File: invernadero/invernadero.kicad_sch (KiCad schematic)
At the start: 0 parts

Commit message: placa con conexiones para display y botonera
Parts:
- added J1, J2: Conn_02x20_Odd_Even, Connector_PinSocket_2.54mm:PinSocket_2x20_P2.54mm_Vertical, symbol Connector_Generic:Conn_02x20_Odd_Even
- added J3: Conn_01x08_Pin, Connector_PinHeader_2.54mm:PinHeader_1x08_P2.54mm_Vertical, symbol Connector:Conn_01x08_Pin
- added J4: Conn_01x16_Socket, Connector_PinSocket_2.54mm:PinSocket_1x16_P2.54mm_Vertical, symbol Connector:Conn_01x16_Socket
- added R1: 1k, Resistor_THT:R_Axial_DIN0207_L6.3mm_D2.5mm_P10.16mm_Horizontal, symbol Device:R
- added RV1: R_Potentiometer_Trim, Potentiometer_THT:Potentiometer_Bourns_3386P_Vertical, symbol Device:R_Potentiometer_Trim
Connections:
- new net: J4.15 (Pin_15), R1.1
- new net: J4.3 (Pin_3), RV1.2
- new net: J1.3 (Pin_3), J3.1 (Pin_1)
- new net: J1.1 (Pin_1), J3.2 (Pin_2)
- new net: J1.2 (Pin_2), J3.3 (Pin_3)
- new net: J1.4 (Pin_4), J3.4 (Pin_4)
- new net: J1.36 (Pin_36), J3.5 (Pin_5)
- new net: J1.38 (Pin_38), J3.6 (Pin_6)
- new net: J1.37 (Pin_37), J3.7 (Pin_7)
- new net: J1.35 (Pin_35), J3.8 (Pin_8)
- new net +5V: J1.17 (Pin_17), J4.2 (Pin_2), R1.2, RV1.3
- new net GND: J1.20 (Pin_20), J1.7 (Pin_7), J2.10 (Pin_10), J2.19 (Pin_19), J4.1 (Pin_1), J4.16 (Pin_16), J4.5 (Pin_5), RV1.1
- new net PA8: J2.24 (Pin_24), J4.11 (Pin_11)
- new net PA9: J2.22 (Pin_22), J4.6 (Pin_6)
- new net PB10: J2.26 (Pin_26), J4.12 (Pin_12)
- new net PB4: J2.28 (Pin_28), J4.13 (Pin_13)
- new net PB5: J2.30 (Pin_30), J4.14 (Pin_14)
- new net PC7: J2.20 (Pin_20), J4.4 (Pin_4)
- no-connect marks 0 -> 6
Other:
- note added: "Display"

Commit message: Diseño de PCB completo
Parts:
- added D1: LED, LED_THT:LED_D4.0mm, symbol Device:LED
- added D2: D, Diode_THT:D_DO-41_SOD81_P7.62mm_Horizontal, symbol Device:D
- added J5: Conn_01x04_Socket, Connector_PinSocket_2.54mm:PinSocket_1x04_P2.54mm_Vertical, symbol Connector:Conn_01x04_Socket
- added J6, J7, J9: Conn_01x02_Socket, Connector_PinSocket_2.54mm:PinSocket_1x02_P2.54mm_Vertical, symbol Connector:Conn_01x02_Socket
- added J8: Conn_01x03_Socket, Connector_PinSocket_2.54mm:PinSocket_1x03_P2.54mm_Vertical, symbol Connector:Conn_01x03_Socket
- added Q1: NPN, Package_TO_SOT_THT:TO-92_Inline, symbol Simulation_SPICE:NPN
- added R2, R3: 3.3k, Resistor_THT:R_Axial_DIN0204_L3.6mm_D1.6mm_P5.08mm_Horizontal, symbol Device:R
- added R4: 27k, Resistor_THT:R_Axial_DIN0207_L6.3mm_D2.5mm_P7.62mm_Horizontal, symbol Device:R
- added R5: 1.2k, Resistor_THT:R_Axial_DIN0207_L6.3mm_D2.5mm_P7.62mm_Horizontal, symbol Device:R
- added R6, R7, R8: R, Resistor_THT:R_Axial_DIN0204_L3.6mm_D1.6mm_P5.08mm_Horizontal, symbol Device:R
- R1: footprint Resistor_THT:R_Axial_DIN0207_L6.3mm_D2.5mm_P10.16mm_Horizontal -> Resistor_THT:R_Axial_DIN0204_L3.6mm_D1.6mm_P5.08mm_Horizontal
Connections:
- net GND: now also D1.1 (K), J5.2 (Pin_2), J8.3 (Pin_3), Q1.3 (E), R4.2, R5.2, R8.2
- net PC8: now reaches J2.1 (Pin_1)
- net PC8: now also R6.1
- net PC9: now reaches J2.2 (Pin_2)
- net PC9: now also R7.1
- net PB8: now reaches J2.4 (Pin_4)
- net PB8: now also J5.3 (Pin_3), R3.2
- net PB9: now reaches J2.6 (Pin_6)
- net PB9: now also J5.4 (Pin_4), R2.2
- net PD2: now reaches J1.3 (Pin_3), J3.1 (Pin_1)
- net PC11: now reaches J1.1 (Pin_1), J3.2 (Pin_2)
- net PC10: now reaches J1.2 (Pin_2), J3.3 (Pin_3)
- net PC12: now reaches J1.4 (Pin_4), J3.4 (Pin_4)
- net PC2: now reaches J1.36 (Pin_36), J3.5 (Pin_5)
- net PC3: now reaches J1.38 (Pin_38), J3.6 (Pin_6)
- net PC0: now reaches J1.37 (Pin_37), J3.7 (Pin_7)
- net PC1: now reaches J1.35 (Pin_35), J3.8 (Pin_8)
- net +3.3V: now reaches J1.15 (Pin_15)
- net +3.3V: now also J5.1 (Pin_1), J6.1 (Pin_1), J7.1 (Pin_1), J8.2 (Pin_2), R2.1, R3.1
- net PA0: now reaches J1.27 (Pin_27)
- net PA0: now also J6.2 (Pin_2), R5.1
- net PA1: now reaches J1.29 (Pin_29)
- net PA1: now also J8.1 (Pin_1)
- net PA4: now reaches J1.31 (Pin_31)
- net PA4: now also J7.2 (Pin_2), R4.1
- new net: Q1.2 (B), R7.2, R8.1
- new net: D1.2 (A), R6.2
- new net: D2.2 (A), J9.2 (Pin_2), Q1.1 (C)
- new net +12V: D2.1 (K), J9.1 (Pin_1)
- no-connect marks 6 -> 8
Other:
- note added: "AT24C08"
- note added: "Humedad"
- note added: "Keypad"
- note added: "Luz"
- note added: "Sensores"
- note added: "Temperatura"
- moved on the sheet: J3, J4, R1, RV1

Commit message: esquemático
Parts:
- added J10: Conn_01x02_Socket, TerminalBlock_CUI:TerminalBlock_CUI_TB007-508-02_1x02_P5.08mm_Horizontal, symbol Connector:Conn_01x02_Socket
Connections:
- net +12V: now also J10.1 (Pin_1)
- net GND: now also J10.2 (Pin_2)
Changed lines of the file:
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@@
+	(wire
+		(pts
+			(xy 227.33 158.75) (xy 229.87 158.75)
+		)
+		(stroke
+			(width 0)
+			(type default)
+		)
+	)
 	(wire
 		(pts
@@
 		(pts
 			(xy 207.01 158.75) (xy 207.01 161.29)
+		)
+		(stroke
+			(width 0)
+			(type default)
+		)
+	)
+	(wire
+		(pts
+			(xy 227.33 156.21) (xy 229.87 156.21)
 		)
 		(stroke
@@
 	)
 	(symbol
+		(lib_id "Connector:Conn_01x02_Socket")
+		(at 234.95 156.21 0)
+		(unit 1)
+		(exclude_from_sim no)
+		(in_bom yes)
+		(on_board yes)
+		(dnp no)
+		(fields_autoplaced yes)
+		(property "Reference" "J10"
+			(at 235.6612 156.2678 0)
+			(effects
+				(font
+					(size 1.27 1.27)
+				)
+				(justify left)
+			)
+		)
+		(property "Value" "Conn_01x02_Socket"
+			(at 235.6612 158.6921 0)
+			(effects
+				(font
+					(size 1.27 1.27)
+				)
+				(justify left)
+			)
+		)
+		(property "Footprint" "TerminalBlock_CUI:TerminalBlock_CUI_TB007-508-02_1x02_P5.08mm_Horizontal"
+			(at 234.95 156.21 0)
+			(effects
+				(font
+					(size 1.27 1.27)
+				)
+				(hide yes)
+			)
+		)
+		(property "Datasheet" "~"
+			(at 234.95 156.21 0)
+			(effects
+				(font
+					(size 1.27 1.27)
+				)
+				(hide yes)
+			)
+		)
+		(property "Description" "Generic connector, single row, 01x02, script generated"
+			(at 234.95 156.21 0)
+			(effects
+				(font
+					(size 1.27 1.27)
+				)
+				(hide yes)
+			)
+		)
+		(pin "2"
+		)
+		(pin "1"
+		)
+		(instances
+			(project ""
+				(path "/aeacc457-9040-4f3b-92d7-10d03e7d1e75"
+					(reference "J10")
+					(unit 1)
+				)
+			)
+		)
+	)
+	(symbol
 		(lib_id "Device:R")
 		(at 177.8 137.16 0)
@@
 	)
 	(symbol
+		(lib_id "power:+12V")
+		(at 227.33 156.21 0)
+		(unit 1)
+		(exclude_from_sim no)
+		(in_bom yes)
+		(on_board yes)
+		(dnp no)
+		(fields_autoplaced yes)
+		(property "Reference" "#PWR025"
+			(at 227.33 160.02 0)
+			(effects
+				(font
+					(size 1.27 1.27)
+				)
+				(hide yes)
+			)
+		)
+		(property "Value" "+12V"
+			(at 227.33 152.0769 0)
+			(effects
+				(font
+					(size 1.27 1.27)
+				)
+			)
+		)
+		(property "Footprint" ""
+			(at 227.33 156.21 0)
+			(effects
+				(font
+					(size 1.27 1.27)
+				)
+				(hide yes)
+			)
+		)
+		(property "Datasheet" ""
+			(at 227.33 156.21 0)
+			(effects
+				(font
+					(size 1.27 1.27)
+				)
+				(hide yes)
+			)
+		)
+		(property "Description" "Power symbol creates a global label with name \"+12V\""
+			(at 227.33 156.21 0)
+			(effects
+				(font
+					(size 1.27 1.27)
+				)
+				(hide yes)
+			)
+		)
+		(pin "1"
+		)
+		(instances
+			(project "invernadero"
+				(path "/aeacc457-9040-4f3b-92d7-10d03e7d1e75"
+					(reference "#PWR025")
+					(unit 1)
+				)
+			)
+		)
+	)
+	(symbol
 		(lib_id "Device:R_Potentiometer_Trim")
 		(at 138.43 143.51 180)
@@
 					(unit 1)
 				)
+			)
+		)
+	)
+	(symbol
+		(lib_id "power:GND")
+		(at 227.33 158.75 0)
+		(unit 1)
+		(exclude_from_sim no)
+		(in_bom yes)
+		(on_board yes)
+		(dnp no)
+		(fields_autoplaced yes)
+		(property "Reference" "#PWR026"
+			(at 227.33 165.1 0)
+			(effects
+				(font
+					(size 1.27 1.27)
+				)
+				(hide yes)
+			)
+		)
+		(property "Value" "GND"
+			(at 227.33 162.8831 0)
+			(effects
+				(font
+					(size 1.27 1.27)
+				)
+			)
+		)
+		(property "Footprint" ""
+			(at 227.33 158.75 0)
+			(effects
+				(font
+					(size 1.27 1.27)
+				)
+				(hide yes)
+			)
+		)
+		(property "Datasheet" ""
+			(at 227.33 158.75 0)
+			(effects
+				(font
+					(size 1.27 1.27)
+				)
+				(hide yes)
+			)
+		)
+		(property "Description" "Power symbol creates a global label with name \"GND\" , ground"
+			(at 227.33 158.75 0)
+			(effects
+				(font
+					(size 1.27 1.27)
+				)
+				(hide yes)
+			)
+		)
+		(pin "1"
+		)
+		(instances
+			(project "invernadero"
+				(path "/aeacc457-9040-4f3b-92d7-10d03e7d1e75"
+					(reference "#PWR026")
+					(unit 1)
+				)

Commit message: cambios en el pcb
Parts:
- added R9: 220k, Resistor_THT:R_Axial_DIN0207_L6.3mm_D2.5mm_P7.62mm_Horizontal, symbol Device:R
- J9: footprint Connector_PinSocket_2.54mm:PinSocket_1x02_P2.54mm_Vertical -> TerminalBlock_CUI:TerminalBlock_CUI_TB007-508-02_1x02_P5.08mm_Horizontal
- R6: value R -> 3.3k
- R7, R8: value R -> 1k
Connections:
- net GND: now also R9.1; no longer R8.2
- net at R7.2, R8.1: no longer Q1.2 (B)
- new net: Q1.2 (B), R8.2, R9.2
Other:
- moved on the sheet: D2, J10, J9, Q1, R7, R8

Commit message: Modificado footprint de led y path de fan más ancho
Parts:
- D1: footprint LED_THT:LED_D4.0mm -> LED_THT:LED_D3.0mm_Clear
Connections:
- net fan-: now reaches D2.2 (A), J9.2 (Pin_2), Q1.1 (C)
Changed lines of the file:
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@@
+		)
+	)
+	(label "fan-"
+		(at 224.79 142.24 0)
+		(effects
+			(font
+				(size 1.27 1.27)
+			)
+			(justify left bottom)
 		)
 	)
@@
 			)
 		)
-		(property "Footprint" "LED_THT:LED_D4.0mm"
+		(property "Footprint" "LED_THT:LED_D3.0mm_Clear"
 			(at 177.8 147.32 0)
 			(effects

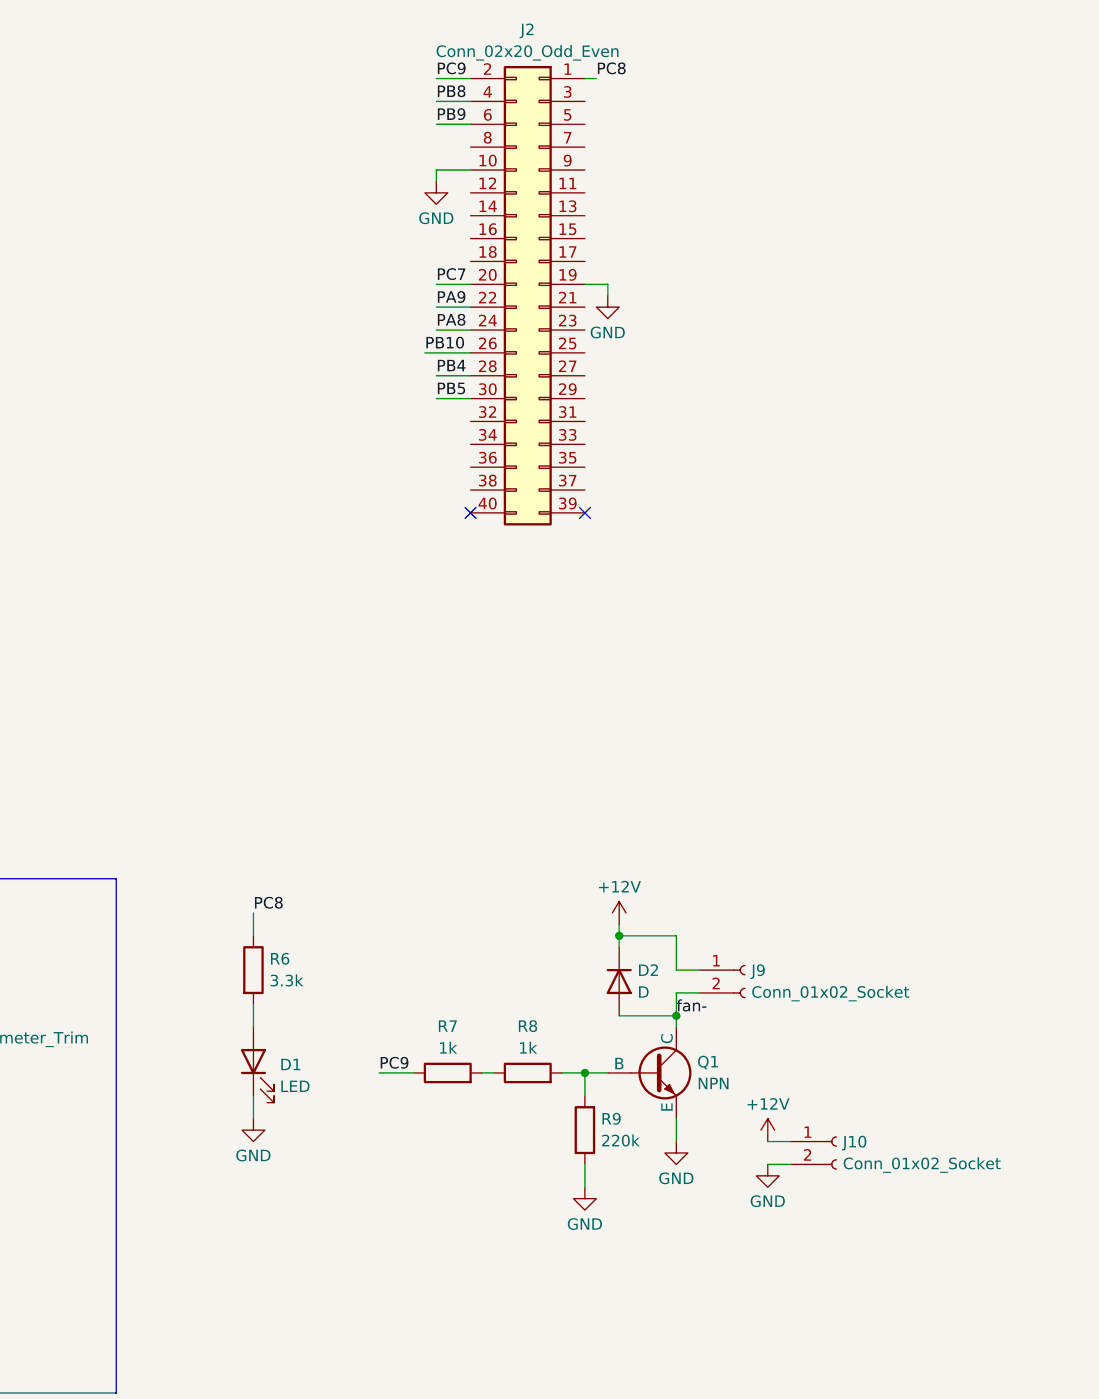
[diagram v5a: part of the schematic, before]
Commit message: Lógica del controlador implementada. Añadido panel de luz. Configuración guarda horas diarias de luz, valor mínimo de luz y temperaturas por día/noche. PCB actualizado.
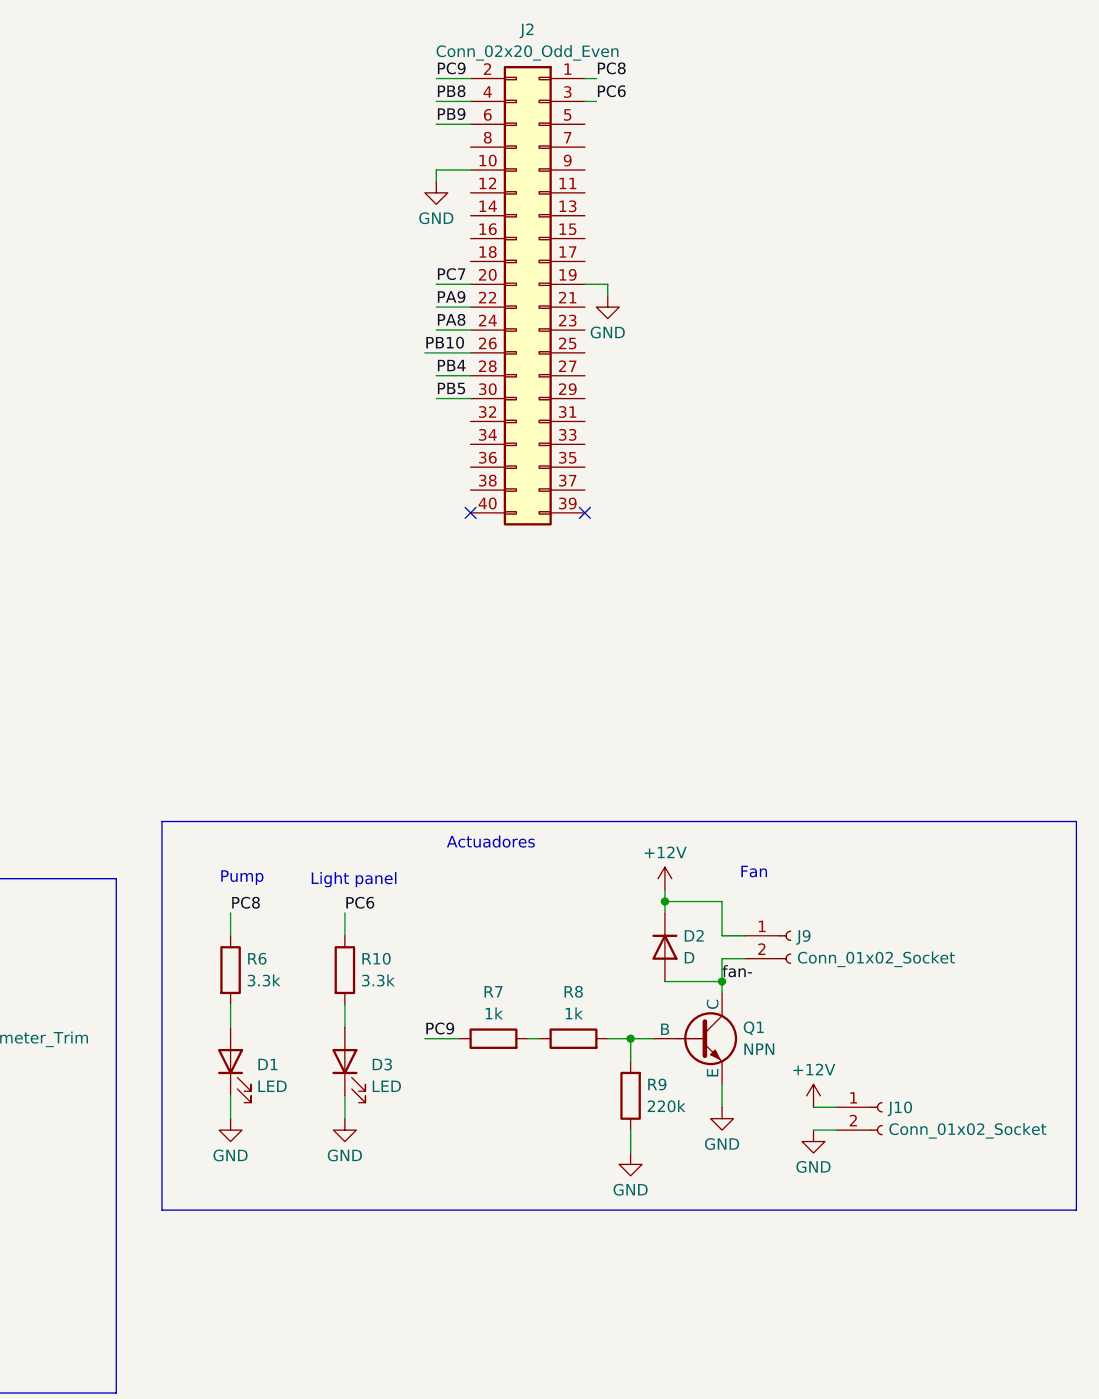
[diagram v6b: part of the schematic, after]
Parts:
- added D3: LED, LED_THT:LED_D3.0mm_Clear, symbol Device:LED
- added R10: 3.3k, Resistor_THT:R_Axial_DIN0204_L3.6mm_D1.6mm_P5.08mm_Horizontal, symbol Device:R
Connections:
- net GND: now also D3.1 (K)
- net PC6: now reaches J2.3 (Pin_3)
- net PC6: now also R10.1
- new net: D3.2 (A), R10.2
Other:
- note added: "Actuadores"
- note added: "Fan"
- note added: "Light panel"
- note added: "Pump"
- moved on the sheet: D1, D2, J10, J9, Q1, R6, R7, R8, R9

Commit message: PCB reordenado. Pistas ensanchadas.
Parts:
- Q1: footprint Package_TO_SOT_THT:TO-92_Inline -> Package_TO_SOT_THT:TO-92_Inline_Wide
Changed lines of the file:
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@@
 			)
 		)
-		(property "Footprint" "Package_TO_SOT_THT:TO-92_Inline"
+		(property "Footprint" "Package_TO_SOT_THT:TO-92_Inline_Wide"
 			(at 290.83 144.78 0)
 			(effects

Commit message: PCB actualizado
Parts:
- added R11, R12, R13: 560k, Resistor_THT:R_Axial_DIN0207_L6.3mm_D2.5mm_P7.62mm_Horizontal, symbol Device:R
- R5: value 1.2k -> 4.7k
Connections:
- net +3.3V: now also J8.1 (Pin_1), R11.1, R12.1, R13.1; no longer J8.2 (Pin_2)
- net GND: now also J8.2 (Pin_2); no longer J8.3 (Pin_3)
- net PA0: now also R11.2
- net PA1: now also J8.3 (Pin_3), R13.2; no longer J8.1 (Pin_1)
- net PA4: now also R12.2
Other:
- moved on the sheet: D1, D2, D3, J10, J3, J4, J5, J6, J7, J8, J9, Q1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
